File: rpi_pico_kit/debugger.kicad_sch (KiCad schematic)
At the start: 48 parts, among them J2 USB_B, U2 NCP1117-3.3_SOT223, U3 RP2040, U4 W25Q16JVSSIQ, U5 74HC14, Y1 12MHz

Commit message: changed footprints from 0805 to 0603
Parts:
- C10, C11, C12, C13, C15, C18, C4, C5, C7, C8, C9: footprint Capacitor_SMD:C_0805_2012Metric_Pad1.18x1.45mm_HandSolder -> Capacitor_SMD:C_0603_1608Metric_Pad1.08x0.95mm_HandSolder; Supplier Part URL https://www.digikey.cz/en/products/detail/kemet/C0805C104M3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 -> (none)
- C16, C17: footprint Capacitor_SMD:C_0805_2012Metric_Pad1.18x1.45mm_HandSolder -> Capacitor_SMD:C_0603_1608Metric_Pad1.08x0.95mm_HandSolder; Supplier Part URL https://www.digikey.cz/en/products/detail/kemet/C0805C120J1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 -> (none)
- R13, R14, R15, R17, R18, R7, R8: footprint Resistor_SMD:R_0805_2012Metric_Pad1.20x1.40mm_HandSolder -> Resistor_SMD:R_0603_1608Metric_Pad0.98x0.95mm_HandSolder; Supplier Part URL https://www.digikey.cz/en/products/detail/yageo/RC0805FR-07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 -> (none)
- R16: footprint Resistor_SMD:R_0805_2012Metric_Pad1.20x1.40mm_HandSolder -> Resistor_SMD:R_0603_1608Metric_Pad0.98x0.95mm_HandSolder; Supplier Part URL https://www.digikey.cz/en/products/detail/yageo/RC0805FR-13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 -> (none)

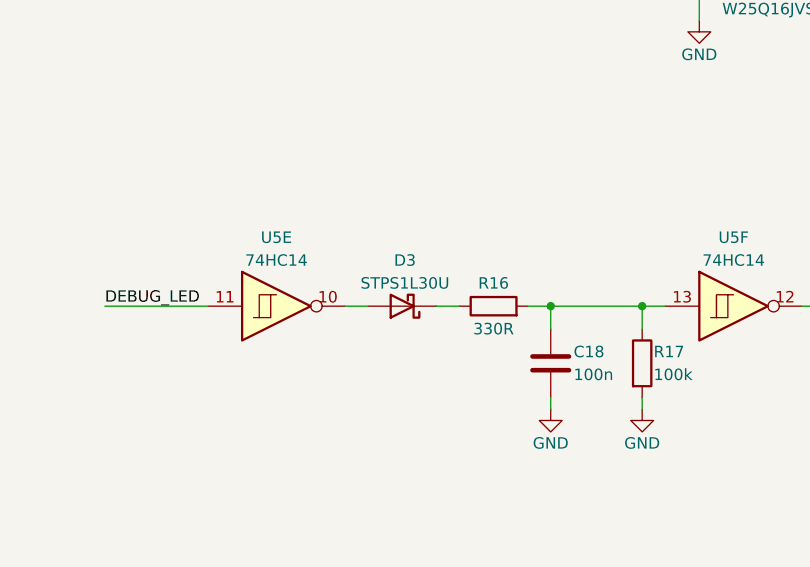
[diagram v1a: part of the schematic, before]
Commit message: changed footprint for diodes
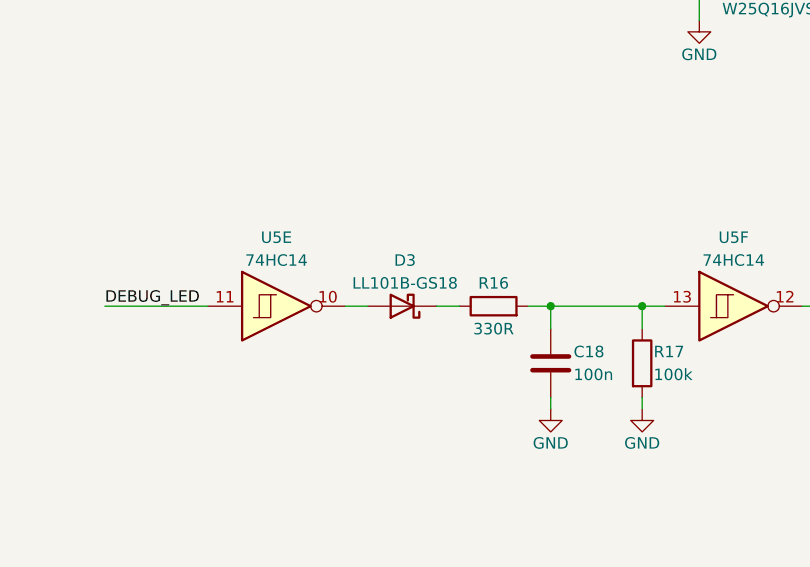
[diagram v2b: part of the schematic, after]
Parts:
- D3: value STPS1L30U -> LL101B-GS18; footprint Diode_SMD:D_SMB -> Diode_SMD:D_MiniMELF; Manufacturer Part Number STPS1L30U -> LL101B-GS18; Supplier Part URL https://www.digikey.cz/en/products/detail/stmicroelectronic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 -> https://www.digikey.cz/en/products/detail/vishay-general-se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
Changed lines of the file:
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@@
       (effects (font (size 1.27 1.27)))
     )
-    (property "Value" "STPS1L30U" (id 1) (at 214.9475 139.7 0)
+    (property "Value" "LL101B-GS18" (id 1) (at 214.9475 139.7 0)
       (effects (font (size 1.27 1.27)))
     )
-    (property "Footprint" "Diode_SMD:D_SMB" (id 2) (at 214.63 142.24 0)
+    (property "Footprint" "Diode_SMD:D_MiniMELF" (id 2) (at 214.63 142.24 0)
       (effects (font (size 1.27 1.27)) hide)
     )
@@
       (effects (font (size 1.27 1.27)) hide)
     )
-    (property "Manufacturer Part Number" "STPS1L30U" (id 4) (at 214.63 142.24 0)
+    (property "Manufacturer Part Number" "LL101B-GS18" (id 4) (at 214.63 142.24 0)
       (effects (font (size 1.27 1.27)) hide)
     )
@@
       (effects (font (size 1.27 1.27)) hide)
     )
-    (property "Supplier Part URL" "https://www.digikey.cz/en/products/detail/stmicroelectronics/STPS1L30U/603493" (id 6) (at 214.63 142.24 0)
+    (property "Supplier Part URL" "https://www.digikey.cz/en/products/detail/vishay-general-semiconductor-diodes-division/LL101B-GS18/4828967" (id 6) (at 214.63 142.24 0)
       (effects (font (size 1.27 1.27)) hide)
     )

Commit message: pcb changes
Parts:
- removed JP2, JP3, JP4, JP5, JP6: SolderJumper_2_Bridged, Jumper:SolderJumper-2_P1.3mm_Bridged_RoundedPad1.0x1.5mm, symbol Jumper:SolderJumper_2_Bridged
- TP3: footprint TestPoint:TestPoint_Pad_D1.5mm -> TestPoint:TestPoint_Pad_D1.0mm
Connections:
- net SWCLK: now also RN14.6 (R3.2)
- net SWDIO: now also RN14.5 (R4.2)
- net UART_RX: now also U3.7 (GPIO5)
- net UART_TX: now also U3.6 (GPIO4)
- net ~{RESET}: now also R13.2
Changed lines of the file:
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@@
-    (stroke (width 0) (type default))
-  )
-  (wire (pts (xy 109.22 90.17) (xy 132.08 90.17))
     (stroke (width 0) (type default))
   )
@@
     (stroke (width 0) (type default))
   )
-  (wire (pts (xy 139.7 90.17) (xy 143.51 90.17))
+  (wire (pts (xy 109.22 90.17) (xy 129.54 90.17))
     (stroke (width 0) (type default))
   )
@@
     (stroke (width 0) (type default))
   )
-  (wire (pts (xy 124.46 92.71) (xy 132.08 92.71))
-    (stroke (width 0) (type default))
-  )
   (wire (pts (xy 260.35 102.87) (xy 274.32 102.87))
     (stroke (width 0) (type default))
@@
     (stroke (width 0) (type default))
   )
-  (wire (pts (xy 139.7 85.09) (xy 143.51 85.09))
+  (wire (pts (xy 124.46 85.09) (xy 129.54 85.09))
     (stroke (width 0) (type default))
   )
@@
     (stroke (width 0) (type default))
   )
-  (wire (pts (xy 139.7 82.55) (xy 143.51 82.55))
-    (stroke (width 0) (type default))
-  )
   (wire (pts (xy 33.02 118.11) (xy 45.72 118.11))
     (stroke (width 0) (type default))
@@
     (stroke (width 0) (type default))
   )
-  (wire (pts (xy 124.46 85.09) (xy 132.08 85.09))
-    (stroke (width 0) (type default))
-  )
   (wire (pts (xy 57.15 43.18) (xy 57.15 57.15))
     (stroke (width 0) (type default))
@@
     (stroke (width 0) (type default))
   )
-  (wire (pts (xy 139.7 87.63) (xy 143.51 87.63))
+  (wire (pts (xy 109.22 87.63) (xy 129.54 87.63))
     (stroke (width 0) (type default))
   )
@@
     (stroke (width 0) (type default))
   )
-  (wire (pts (xy 124.46 82.55) (xy 132.08 82.55))
+  (wire (pts (xy 124.46 82.55) (xy 129.54 82.55))
     (stroke (width 0) (type default))
   )
@@
     (stroke (width 0) (type default))
   )
-  (wire (pts (xy 109.22 87.63) (xy 132.08 87.63))
-    (stroke (width 0) (type default))
-  )
   (wire (pts (xy 124.46 29.21) (xy 113.03 29.21))
     (stroke (width 0) (type default))
@@
     (stroke (width 0) (type default))
   )
-  (wire (pts (xy 139.7 92.71) (xy 143.51 92.71))
+  (wire (pts (xy 124.46 92.71) (xy 129.54 92.71))
     (stroke (width 0) (type default))
   )
@@
     (effects (font (size 1.27 1.27)) (justify left bottom))
   )
-  (hierarchical_label "UART_TX" (shape output) (at 143.51 87.63 0) (fields_autoplaced)
+  (hierarchical_label "UART_TX" (shape output) (at 129.54 87.63 0) (fields_autoplaced)
     (effects (font (size 1.27 1.27)) (justify left))
   )
-  (hierarchical_label "SWCLK" (shape output) (at 143.51 82.55 0) (fields_autoplaced)
+  (hierarchical_label "SWCLK" (shape output) (at 129.54 82.55 0) (fields_autoplaced)
     (effects (font (size 1.27 1.27)) (justify left))
   )
-  (hierarchical_label "UART_RX" (shape input) (at 143.51 90.17 0) (fields_autoplaced)
+  (hierarchical_label "UART_RX" (shape input) (at 129.54 90.17 0) (fields_autoplaced)
     (effects (font (size 1.27 1.27)) (justify left))
   )
-  (hierarchical_label "SWDIO" (shape bidirectional) (at 143.51 85.09 0) (fields_autoplaced)
+  (hierarchical_label "SWDIO" (shape bidirectional) (at 129.54 85.09 0) (fields_autoplaced)
     (effects (font (size 1.27 1.27)) (justify left))
   )
-  (hierarchical_label "~{RESET}" (shape output) (at 143.51 92.71 0) (fields_autoplaced)
+  (hierarchical_label "~{RESET}" (shape output) (at 129.54 92.71 0) (fields_autoplaced)
     (effects (font (size 1.27 1.27)) (justify left))
   )
@@
       (effects (font (size 1.27 1.27)) (justify left))
     )
-    (property "Footprint" "TestPoint:TestPoint_Pad_D1.5mm" (id 2) (at 133.35 76.2 0)
+    (property "Footprint" "TestPoint:TestPoint_Pad_D1.0mm" (id 2) (at 133.35 76.2 0)
       (effects (font (size 1.27 1.27)) hide)
     )
@@
     (pin "1")
   )
-  (symbol (lib_id "Jumper:SolderJumper_2_Bridged") (at 135.89 92.71 0) (unit 1)
-    (in_bom yes) (on_board yes)
-    (property "Reference" "JP6" (id 0) (at 130.81 91.44 0)
-      (effects (font (size 1.27 1.27)))
-    )
-    (property "Value" "SolderJumper_2_Bridged" (id 1) (at 135.89 90.17 0)
-      (effects (font (size 1.27 1.27)) hide)
-    )
-    (property "Footprint" "Jumper:SolderJumper-2_P1.3mm_Bridged_RoundedPad1.0x1.5mm" (id 2) (at 135.89 92.71 0)
-      (effects (font (size 1.27 1.27)) hide)
-    )
-    (property "Datasheet" "~" (id 3) (at 135.89 92.71 0)
-      (effects (font (size 1.27 1.27)) hide)
-    )
-    (property "Manufacturer Part Number" "~" (id 4) (at 135.89 92.71 0)
-      (effects (font (size 1.27 1.27)) hide)
-    )
-    (property "Supplier" "~" (id 5) (at 135.89 92.71 0)
-      (effects (font (size 1.27 1.27)) hide)
-    )
-    (property "Supplier Part URL" "~" (id 6) (at 135.89 92.71 0)
-      (effects (font (size 1.27 1.27)) hide)
-    )
-    (pin "1")
-    (pin "2")
-  )
   (symbol (lib_id "Device:R") (at 214.63 95.25 90) (unit 1)
     (in_bom yes) (on_board yes)
@@
     )
     (property "Supplier Part URL" "" (id 6) (at 135.89 34.29 0)
-      (effects (font (size 1.27 1.27)) hide)
-    )
-    (pin "1")
-    (pin "2")
-  )
-  (symbol (lib_id "Jumper:SolderJumper_2_Bridged") (at 135.89 82.55 0) (unit 1)
-    (in_bom yes) (on_board yes)
-    (property "Reference" "JP2" (id 0) (at 130.81 81.28 0)
-      (effects (font (size 1.27 1.27)))
-    )
-    (property "Value" "SolderJumper_2_Bridged" (id 1) (at 135.89 80.01 0)
-      (effects (font (size 1.27 1.27)) hide)
-    )
-    (property "Footprint" "Jumper:SolderJumper-2_P1.3mm_Bridged_RoundedPad1.0x1.5mm" (id 2) (at 135.89 82.55 0)
-      (effects (font (size 1.27 1.27)) hide)
-    )
-    (property "Datasheet" "~" (id 3) (at 135.89 82.55 0)
-      (effects (font (size 1.27 1.27)) hide)
-    )
-    (property "Manufacturer Part Number" "~" (id 4) (at 135.89 82.55 0)
-      (effects (font (size 1.27 1.27)) hide)
-    )
-    (property "Supplier" "~" (id 5) (at 135.89 82.55 0)
-      (effects (font (size 1.27 1.27)) hide)
-    )
-    (property "Supplier Part URL" "~" (id 6) (at 135.89 82.55 0)
       (effects (font (size 1.27 1.27)) hide)
     )
@@
     )
     (pin "1")
-  )
-  (symbol (lib_id "Jumper:SolderJumper_2_Bridged") (at 135.89 90.17 0) (unit 1)
-    (in_bom yes) (on_board yes)
-    (property "Reference" "JP5" (id 0) (at 130.81 88.9 0)
-      (effects (font (size 1.27 1.27)))
-    )
-    (property "Value" "SolderJumper_2_Bridged" (id 1) (at 135.89 87.63 0)
-      (effects (font (size 1.27 1.27)) hide)
-    )
-    (property "Footprint" "Jumper:SolderJumper-2_P1.3mm_Bridged_RoundedPad1.0x1.5mm" (id 2) (at 135.89 90.17 0)
-      (effects (font (size 1.27 1.27)) hide)
-    )
-    (property "Datasheet" "~" (id 3) (at 135.89 90.17 0)
-      (effects (font (size 1.27 1.27)) hide)
-    )
-    (property "Manufacturer Part Number" "~" (id 4) (at 135.89 90.17 0)
-      (effects (font (size 1.27 1.27)) hide)
-    )
-    (property "Supplier" "~" (id 5) (at 135.89 90.17 0)
-      (effects (font (size 1.27 1.27)) hide)
-    )
-    (property "Supplier Part URL" "~" (id 6) (at 135.89 90.17 0)
-      (effects (font (size 1.27 1.27)) hide)
-    )
-    (pin "1")
-    (pin "2")
   )
   (symbol (lib_id "Device:C") (at 124.46 34.29 180) (unit 1)
@@
     )
     (property "Supplier Part URL" "https://www.digikey.cz/en/products/detail/kemet/C0805C105Z4VAC7800/2211782" (id 6) (at 101.6 48.26 0)
-      (effects (font (size 1.27 1.27)) hide)
-    )
-    (pin "1")
-    (pin "2")
-  )
-  (symbol (lib_id "Jumper:SolderJumper_2_Bridged") (at 135.89 87.63 0) (unit 1)
-    (in_bom yes) (on_board yes)
-    (property "Reference" "JP4" (id 0) (at 130.81 86.36 0)
-      (effects (font (size 1.27 1.27)))
-    )
-    (property "Value" "SolderJumper_2_Bridged" (id 1) (at 135.89 85.09 0)
-      (effects (font (size 1.27 1.27)) hide)
-    )
-    (property "Footprint" "Jumper:SolderJumper-2_P1.3mm_Bridged_RoundedPad1.0x1.5mm" (id 2) (at 135.89 87.63 0)
-      (effects (font (size 1.27 1.27)) hide)
-    )
-    (property "Datasheet" "~" (id 3) (at 135.89 87.63 0)
-      (effects (font (size 1.27 1.27)) hide)
-    )
-    (property "Manufacturer Part Number" "~" (id 4) (at 135.89 87.63 0)
-      (effects (font (size 1.27 1.27)) hide)
-    )
-    (property "Supplier" "~" (id 5) (at 135.89 87.63 0)
-      (effects (font (size 1.27 1.27)) hide)
-    )
-    (property "Supplier Part URL" "~" (id 6) (at 135.89 87.63 0)
       (effects (font (size 1.27 1.27)) hide)
     )
@@
     (pin "8")
   )
-  (symbol (lib_id "Jumper:SolderJumper_2_Bridged") (at 135.89 85.09 0) (unit 1)
-    (in_bom yes) (on_board yes)
-    (property "Reference" "JP3" (id 0) (at 130.81 83.82 0)
-      (effects (font (size 1.27 1.27)))
-    )
-    (property "Value" "SolderJumper_2_Bridged" (id 1) (at 135.89 82.55 0)
-      (effects (font (size 1.27 1.27)) hide)
-    )
-    (property "Footprint" "Jumper:SolderJumper-2_P1.3mm_Bridged_RoundedPad1.0x1.5mm" (id 2) (at 135.89 85.09 0)
-      (effects (font (size 1.27 1.27)) hide)
-    )
-    (property "Datasheet" "~" (id 3) (at 135.89 85.09 0)
-      (effects (font (size 1.27 1.27)) hide)
-    )
-    (property "Manufacturer Part Number" "~" (id 4) (at 135.89 85.09 0)
-      (effects (font (size 1.27 1.27)) hide)
-    )
-    (property "Supplier" "~" (id 5) (at 135.89 85.09 0)
-      (effects (font (size 1.27 1.27)) hide)
-    )
-    (property "Supplier Part URL" "~" (id 6) (at 135.89 85.09 0)
-      (effects (font (size 1.27 1.27)) hide)
-    )
-    (pin "1")
-    (pin "2")
-  )
   (symbol (lib_id "power:GND") (at 257.81 53.34 0) (unit 1)

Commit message: changed footprints for resistor arrays
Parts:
- RN14: footprint Resistor_SMD:R_Array_Convex_4x1206 -> Resistor_SMD:R_Array_Convex_4x0603
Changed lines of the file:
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@@
       (effects (font (size 1.27 1.27)) (justify right))
     )
-    (property "Footprint" "Resistor_SMD:R_Array_Convex_4x1206" (id 2) (at 120.65 75.438 90)
+    (property "Footprint" "Resistor_SMD:R_Array_Convex_4x0603" (id 2) (at 120.65 75.438 90)
       (effects (font (size 1.27 1.27)) hide)
     )
@@
       (effects (font (size 1.27 1.27)) (justify right))
     )
-    (property "Footprint" "Resistor_SMD:R_Array_Convex_4x1206" (id 2) (at 120.65 83.058 90)
+    (property "Footprint" "Resistor_SMD:R_Array_Convex_4x0603" (id 2) (at 120.65 83.058 90)
       (effects (font (size 1.27 1.27)) hide)
     )
@@
       (effects (font (size 1.27 1.27)) (justify right))
     )
-    (property "Footprint" "Resistor_SMD:R_Array_Convex_4x1206" (id 2) (at 120.65 77.978 90)
+    (property "Footprint" "Resistor_SMD:R_Array_Convex_4x0603" (id 2) (at 120.65 77.978 90)
       (effects (font (size 1.27 1.27)) hide)
     )
@@
       (effects (font (size 1.27 1.27)) (justify right))
     )
-    (property "Footprint" "Resistor_SMD:R_Array_Convex_4x1206" (id 2) (at 120.65 80.518 90)
-      (effects (font (size 1.27 1.27)) hide)
-    )
+    (property "Footprint" "Resistor_SMD:R_Array_Convex_4x0603" (id 2) (at 120.65 80.518 90)
+      (effects (font (size 1.27 1.27)) hide)
+    )

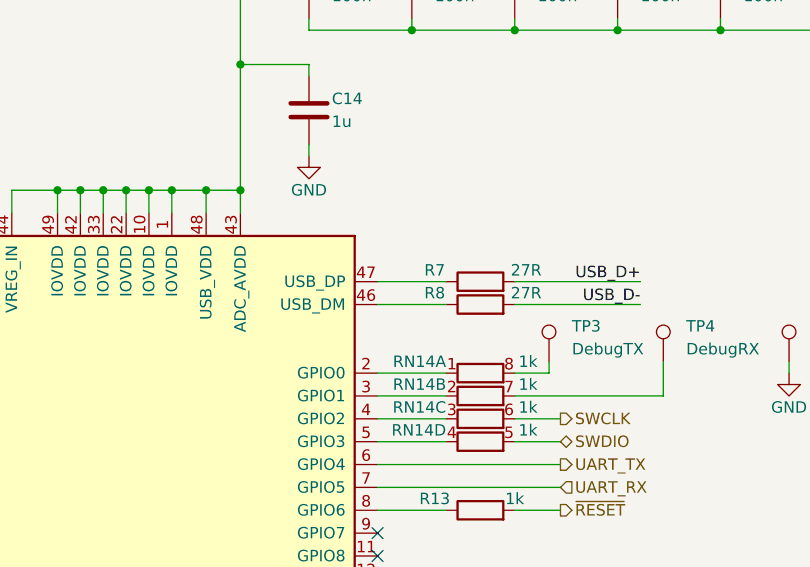
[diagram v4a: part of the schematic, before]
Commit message: added names to differential pairs
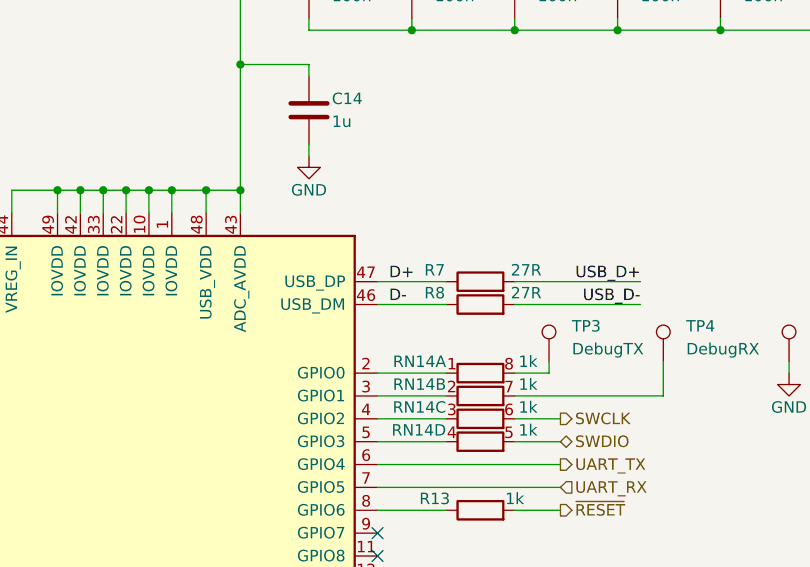
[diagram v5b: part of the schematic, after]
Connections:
- net D-: now reaches R8.1, U3.46 (USB_DM)
- net D+: now reaches R7.1, U3.47 (USB_DP)
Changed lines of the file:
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@@
     (effects (font (size 1.27 1.27)) (justify right bottom))
+  )
+  (label "D-" (at 110.49 69.85 0) (fields_autoplaced)
+    (effects (font (size 1.27 1.27)) (justify left bottom))
   )
   (label "QSPI_SS" (at 33.02 78.74 0) (fields_autoplaced)
@@
     (effects (font (size 1.27 1.27)) (justify right bottom))
   )
+  (label "D+" (at 110.49 67.31 0) (fields_autoplaced)
+    (effects (font (size 1.27 1.27)) (justify left bottom))
+  )
   (label "XOUT" (at 166.37 184.15 0) (fields_autoplaced)

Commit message: debugger (unrouted 163)
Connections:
- net SWCLK: now also RN14.3 (R3.1); no longer RN14.6 (R3.2)
- net SWDIO: now also RN14.4 (R4.1); no longer RN14.5 (R4.2)
- net at RN14.1 (R1.1): now also TP3.1; no longer U3.2 (GPIO0)
- net at RN14.8 (R1.2): now also U3.2 (GPIO0); no longer TP3.1
- net at U3.3 (GPIO1): now also RN14.7 (R2.2); no longer RN14.2 (R2.1)
- net at U3.4 (GPIO2): now also RN14.6 (R3.2); no longer RN14.3 (R3.1)
- net at U3.5 (GPIO3): now also RN14.5 (R4.2); no longer RN14.4 (R4.1)
- net at TP4.1: now also RN14.2 (R2.1); no longer RN14.7 (R2.2)
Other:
- moved on the sheet: RN14A, RN14B, RN14C, RN14D
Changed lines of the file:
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@@
     (effects (font (size 1.27 1.27)) (justify left))
   )
-  (symbol (lib_id "Device:R_Pack04_Split") (at 120.65 77.47 270) (unit 1)
-    (in_bom yes) (on_board yes)
-    (property "Reference" "RN14" (id 0) (at 116.84 76.2 90)
-      (effects (font (size 1.27 1.27)) (justify right))
-    )
-    (property "Value" "1k" (id 1) (at 127 76.2 90)
+  (symbol (lib_id "Device:R_Pack04_Split") (at 120.65 77.47 90) (mirror x) (unit 1)
+    (in_bom yes) (on_board yes)
+    (property "Reference" "RN14" (id 0) (at 124.46 76.2 90)
+      (effects (font (size 1.27 1.27)) (justify right))
+    )
+    (property "Value" "1k" (id 1) (at 114.3 76.2 90)
       (effects (font (size 1.27 1.27)) (justify right))
     )
@@
     (pin "3")
   )
-  (symbol (lib_id "Device:R_Pack04_Split") (at 120.65 85.09 270) (unit 4)
-    (in_bom yes) (on_board yes)
-    (property "Reference" "RN14" (id 0) (at 116.84 83.82 90)
-      (effects (font (size 1.27 1.27)) (justify right))
-    )
-    (property "Value" "1k" (id 1) (at 127 83.82 90)
+  (symbol (lib_id "Device:R_Pack04_Split") (at 120.65 85.09 90) (mirror x) (unit 4)
+    (in_bom yes) (on_board yes)
+    (property "Reference" "RN14" (id 0) (at 124.46 83.82 90)
+      (effects (font (size 1.27 1.27)) (justify right))
+    )
+    (property "Value" "1k" (id 1) (at 114.3 83.82 90)
       (effects (font (size 1.27 1.27)) (justify right))
     )
@@
     (pin "1")
   )
-  (symbol (lib_id "Device:R_Pack04_Split") (at 120.65 80.01 270) (unit 2)
-    (in_bom yes) (on_board yes)
-    (property "Reference" "RN14" (id 0) (at 116.84 78.74 90)
-      (effects (font (size 1.27 1.27)) (justify right))
-    )
-    (property "Value" "1k" (id 1) (at 127 78.74 90)
+  (symbol (lib_id "Device:R_Pack04_Split") (at 120.65 80.01 90) (mirror x) (unit 2)
+    (in_bom yes) (on_board yes)
+    (property "Reference" "RN14" (id 0) (at 124.46 78.74 90)
+      (effects (font (size 1.27 1.27)) (justify right))
+    )
+    (property "Value" "1k" (id 1) (at 114.3 78.74 90)
       (effects (font (size 1.27 1.27)) (justify right))
     )
@@
     (pin "1")
   )
-  (symbol (lib_id "Device:R_Pack04_Split") (at 120.65 82.55 270) (unit 3)
-    (in_bom yes) (on_board yes)
-    (property "Reference" "RN14" (id 0) (at 116.84 81.28 90)
-      (effects (font (size 1.27 1.27)) (justify right))
-    )
-    (property "Value" "1k" (id 1) (at 127 81.28 90)
-      (effects (font (size 1.27 1.27)) (justify right))
-    )
+  (symbol (lib_id "Device:R_Pack04_Split") (at 120.65 82.55 90) (mirror x) (unit 3)
+    (in_bom yes) (on_board yes)
+    (property "Reference" "RN14" (id 0) (at 124.46 81.28 90)
+      (effects (font (size 1.27 1.27)) (justify right))
+    )
+    (property "Value" "1k" (id 1) (at 114.3 81.28 90)
+      (effects (font (size 1.27 1.27)) (justify right))
+    )

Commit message: monostable (unrouted 136)
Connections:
- net DEBUG_LED: now also U5.5; no longer U5.11
- net at C18.2, R16.2, R17.1: now also U5.9; no longer U5.13
- net at D3.2 (A): now also U5.6; no longer U5.10
- net at LED2.1 (K): now also U5.8; no longer U5.12
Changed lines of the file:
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@@
     (pin "2")
   )
-  (symbol (lib_id "74xx:74HC14") (at 251.46 142.24 0) (unit 6)
+  (symbol (lib_id "74xx:74HC14") (at 251.46 142.24 0) (unit 4)
     (in_bom yes) (on_board yes) (fields_autoplaced)
     (property "Reference" "U5" (id 0) (at 251.46 134.62 0)
@@
       (effects (font (size 1.27 1.27)) hide)
     )
-    (pin "12")
-    (pin "13")
+    (pin "8")
+    (pin "9")
   )
   (symbol (lib_id "power:GND") (at 241.3 153.67 0) (unit 1)
@@
     (pin "2")
   )
-  (symbol (lib_id "74xx:74HC14") (at 200.66 142.24 0) (unit 5)
+  (symbol (lib_id "74xx:74HC14") (at 200.66 142.24 0) (unit 3)
     (in_bom yes) (on_board yes) (fields_autoplaced)
     (property "Reference" "U5" (id 0) (at 200.66 134.62 0)
@@
       (effects (font (size 1.27 1.27)) hide)
     )
-    (pin "10")
-    (pin "11")
+    (pin "5")
+    (pin "6")
   )
   (symbol (lib_id "Device:C") (at 101.6 48.26 180) (unit 1)
